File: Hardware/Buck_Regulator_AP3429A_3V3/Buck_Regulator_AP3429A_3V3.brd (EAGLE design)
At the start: 25.4 x 25.4 mm, 51 parts, among them J1 Screw Terminal, J2 POWER_JACKPOWER_JACK_SLOT_COM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, J3 Breakout Headers, U1 AP3429/A

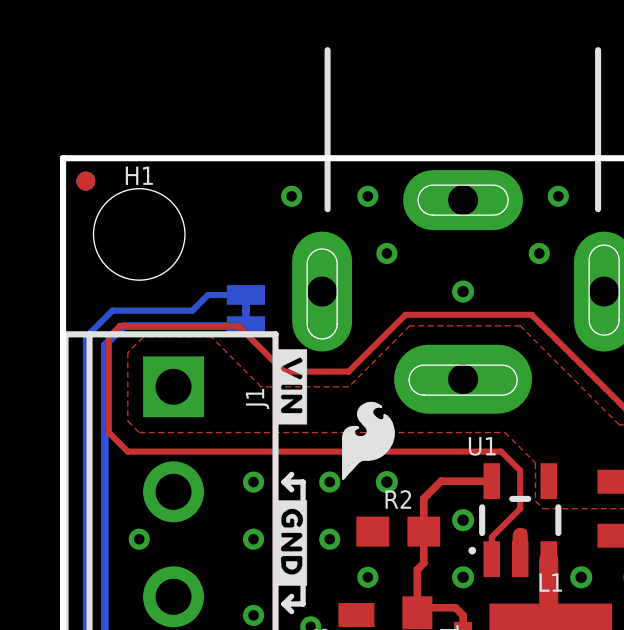
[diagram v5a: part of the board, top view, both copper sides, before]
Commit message: Changed version number in schematic, adjusted components
Moved around some silkscreen in order for easier reading on the backside; changed the version number in the schematic to v10
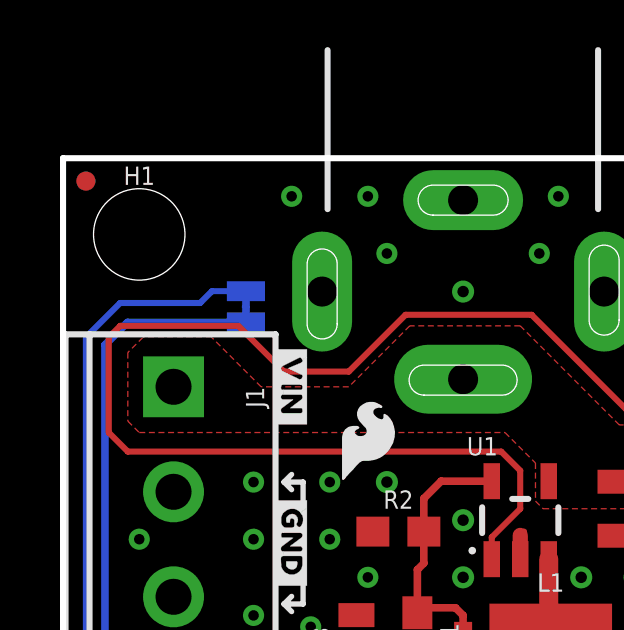
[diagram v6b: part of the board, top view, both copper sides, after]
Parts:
- moved PWR 0.13 mm to (6.10, 20.4)
- moved U$14 0.13 mm to (6.10, 23.2)
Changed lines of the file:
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@@
 <drawing>
 <settings>
-<setting alwaysvectorfont="yes"/>
+<setting alwaysvectorfont="no"/>
 <setting verticaltext="up"/>
 </settings>
@@
 <layer number="37" name="tTest" color="7" fill="1" visible="no" active="yes"/>
 <layer number="38" name="bTest" color="7" fill="1" visible="no" active="yes"/>
-<layer number="39" name="tKeepout" color="4" fill="11" visible="no" active="yes"/>
-<layer number="40" name="bKeepout" color="1" fill="11" visible="no" active="yes"/>
-<layer number="41" name="tRestrict" color="4" fill="10" visible="no" active="yes"/>
-<layer number="42" name="bRestrict" color="1" fill="10" visible="no" active="yes"/>
-<layer number="43" name="vRestrict" color="2" fill="10" visible="no" active="yes"/>
+<layer number="39" name="tKeepout" color="4" fill="11" visible="yes" active="yes"/>
+<layer number="40" name="bKeepout" color="1" fill="11" visible="yes" active="yes"/>
+<layer number="41" name="tRestrict" color="4" fill="10" visible="yes" active="yes"/>
+<layer number="42" name="bRestrict" color="1" fill="10" visible="yes" active="yes"/>
+<layer number="43" name="vRestrict" color="2" fill="10" visible="yes" active="yes"/>
 <layer number="44" name="Drills" color="7" fill="1" visible="no" active="yes"/>
 <layer number="45" name="Holes" color="7" fill="1" visible="yes" active="yes"/>
@@
 <element name="FRAME1" library="SparkFun-Aesthetics" package="CREATIVE_COMMONS" value="FRAME-LEDGER" x="-13.97" y="-41.91" smashed="yes">
 <attribute name="DESIGNER" value="M. Chodikov" x="66.04" y="-54.61" size="1.778" layer="27" display="off"/>
-<attribute name="REV" value="v01" x="66.04" y="-54.61" size="1.778" layer="27" display="off"/>
+<attribute name="REV" value="v10" x="66.04" y="-54.61" size="1.778" layer="27" display="off"/>
 </element>
 <element name="L1" library="SparkFun-Coils" package="INDUCTOR_4X4MM" value="2.2μH" x="16.256" y="8.509" smashed="yes">
@@
 <attribute name="PROD_ID" value="NDUC-13770" x="48.006" y="-15.621" size="1.778" layer="27" display="off"/>
 </element>
-<element name="PWR" library="SparkFun-Jumpers" package="SMT-JUMPER_2_NC_TRACE_SILK" package3d_urn="urn:adsk.eagle:package:39281/1" value="JUMPER-SMT_2_NC_TRACE_SILK" x="6.096" y="20.32" smashed="yes" rot="MR270">
-<attribute name="NAME" x="4.953" y="20.32" size="0.6096" layer="26" font="vector" ratio="20" rot="MR270" align="bottom-center"/>
+<element name="PWR" library="SparkFun-Jumpers" package="SMT-JUMPER_2_NC_TRACE_SILK" package3d_urn="urn:adsk.eagle:package:39281/1" value="JUMPER-SMT_2_NC_TRACE_SILK" x="6.096" y="20.447" smashed="yes" rot="MR270">
+<attribute name="NAME" x="4.953" y="20.447" size="0.6096" layer="26" font="vector" ratio="20" rot="MR270" align="bottom-center"/>
 </element>
 <element name="U1" library="SparkFun-IC-Power" package="SOT23-5" value="AP3429/A" x="15.24" y="13.335" smashed="yes">
@@
 <element name="U$13" library="output" package="#VOUT#3447" value="" x="5.334" y="7.112" smashed="yes" rot="MR90"/>
 <element name="U$15" library="output" package="#VIN#3445" value="" x="5.334" y="17.78" smashed="yes" rot="MR90"/>
-<element name="U$14" library="output" package="#PWR#3451" value="" x="6.096" y="23.114" smashed="yes" rot="MR90"/>
+<element name="U$14" library="output" package="#PWR#3451" value="" x="6.096" y="23.241" smashed="yes" rot="MR90"/>
 <element name="C1" library="SparkFun-Capacitors" package="0805" value="22uF" x="18.415" y="13.716" smashed="yes" rot="R270">
 <attribute name="NAME" x="19.304" y="13.716" size="0.6096" layer="25" font="vector" ratio="20" rot="R270" align="bottom-center"/>
@@
 <signal name="N$3">
 <contactref element="PWR" pad="1"/>
-<wire x1="6.096" y1="20.8407" x2="4.8387" y2="20.8407" width="0.2032" layer="16"/>
-<wire x1="1.651" y1="20.32" x2="0.762" y2="19.431" width="0.2032" layer="16"/>
-<wire x1="4.8387" y1="20.8407" x2="4.318" y2="20.32" width="0.2032" layer="16"/>
-<wire x1="4.318" y1="20.32" x2="1.651" y2="20.32" width="0.2032" layer="16"/>
+<wire x1="6.096" y1="20.9677" x2="4.9657" y2="20.9677" width="0.2032" layer="16"/>
+<wire x1="1.905" y1="20.574" x2="0.762" y2="19.431" width="0.2032" layer="16"/>
+<wire x1="4.9657" y1="20.9677" x2="4.572" y2="20.574" width="0.2032" layer="16"/>
+<wire x1="4.572" y1="20.574" x2="1.905" y2="20.574" width="0.2032" layer="16"/>
 <wire x1="12.485" y1="3.302" x2="13.12" y2="2.667" width="0.2032" layer="1"/>
 <wire x1="12.485" y1="3.302" x2="7.493" y2="3.302" width="0.2032" layer="1"/>
@@
 <contactref element="PWR" pad="2"/>
 <wire x1="1.397" y1="19.177" x2="1.397" y2="9.566" width="0.254" layer="16"/>
-<wire x1="6.096" y1="19.7993" x2="2.0193" y2="19.7993" width="0.254" layer="16"/>
-<wire x1="2.0193" y1="19.7993" x2="1.397" y2="19.177" width="0.254" layer="16"/>
+<wire x1="6.096" y1="19.9263" x2="2.1463" y2="19.9263" width="0.254" layer="16"/>
+<wire x1="2.1463" y1="19.9263" x2="1.397" y2="19.177" width="0.254" layer="16"/>
 <contactref element="L1" pad="P$2"/>
 <contactref element="C2" pad="1"/>

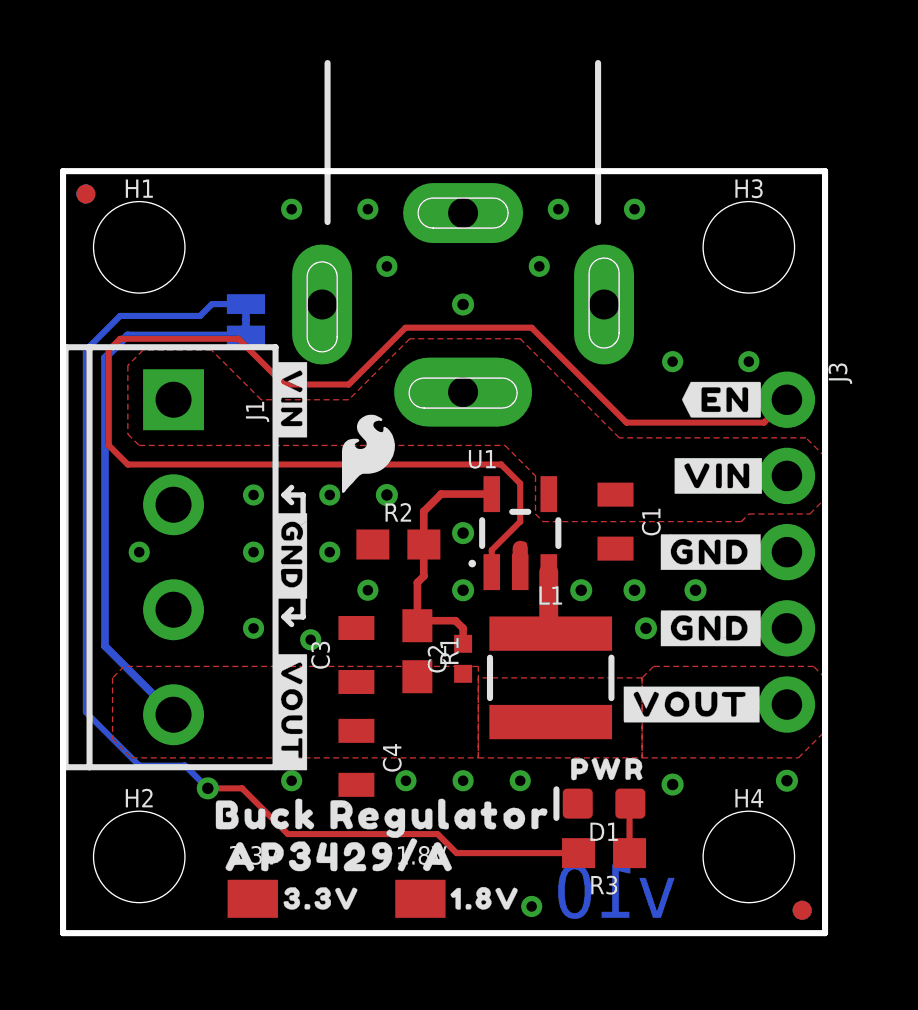
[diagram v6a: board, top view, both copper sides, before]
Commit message: Added 2 more output capacitors
Added more output capacitance to match ALC block - there was some ripple detected during testing so adding these should eliminate that. Adjusted the components on the board accordingly then matched the exact locations of said movement for each board.
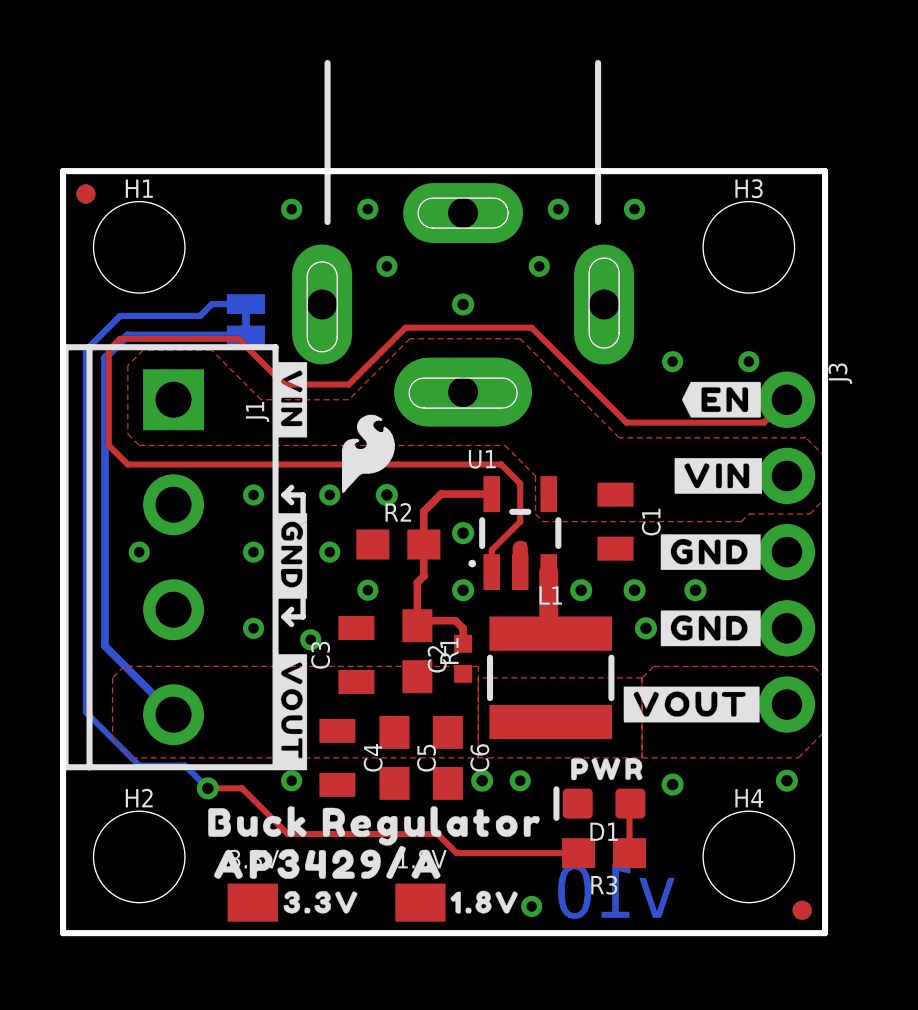
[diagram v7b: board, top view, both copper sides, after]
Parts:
- added C5: 0.1uF, SparkFun-Capacitors:0603
- added C6: 1.0uF, SparkFun-Capacitors:0603
- moved C4 0.63 mm to (9.14, 5.84)
- moved U$3 0.46 mm to (8.89, 2.29)
- moved U$2 0.36 mm to (10.4, 3.68)
- moved 1.8V 0.13 mm to (11.9, 1.02)
- moved 3.3V 0.13 mm to (6.35, 1.02)
- moved U$19 0.13 mm to (14.1, 1.02)
- moved U$23 0.13 mm to (8.64, 1.02)
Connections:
- net GND: now also C5.2, C6.2
- net VOUT: now also C5.1, C6.1
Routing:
- net GND: vias 31 -> 30
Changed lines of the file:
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@@
 <drawing>
 <settings>
-<setting alwaysvectorfont="no"/>
+<setting alwaysvectorfont="yes"/>
 <setting verticaltext="up"/>
 </settings>
@@
 <layer number="37" name="tTest" color="7" fill="1" visible="no" active="yes"/>
 <layer number="38" name="bTest" color="7" fill="1" visible="no" active="yes"/>
-<layer number="39" name="tKeepout" color="4" fill="11" visible="yes" active="yes"/>
-<layer number="40" name="bKeepout" color="1" fill="11" visible="yes" active="yes"/>
-<layer number="41" name="tRestrict" color="4" fill="10" visible="yes" active="yes"/>
-<layer number="42" name="bRestrict" color="1" fill="10" visible="yes" active="yes"/>
-<layer number="43" name="vRestrict" color="2" fill="10" visible="yes" active="yes"/>
+<layer number="39" name="tKeepout" color="4" fill="11" visible="no" active="yes"/>
+<layer number="40" name="bKeepout" color="1" fill="11" visible="no" active="yes"/>
+<layer number="41" name="tRestrict" color="4" fill="10" visible="no" active="yes"/>
+<layer number="42" name="bRestrict" color="1" fill="10" visible="no" active="yes"/>
+<layer number="43" name="vRestrict" color="2" fill="10" visible="no" active="yes"/>
 <layer number="44" name="Drills" color="7" fill="1" visible="no" active="yes"/>
 <layer number="45" name="Holes" color="7" fill="1" visible="yes" active="yes"/>
@@
 <attribute name="VALUE" x="22.098" y="19.05" size="0.6096" layer="27" font="vector" ratio="20" rot="R270"/>
 </element>
-<element name="U$2" library="output" package="BUCK_REGULATOR24" value="" x="10.668" y="3.937" smashed="yes"/>
-<element name="U$3" library="output" package="AP3429#A25" value="" x="9.271" y="2.54" smashed="yes"/>
+<element name="U$2" library="output" package="BUCK_REGULATOR24" value="" x="10.414" y="3.683" smashed="yes"/>
+<element name="U$3" library="output" package="AP3429#A25" value="" x="8.89" y="2.286" smashed="yes"/>
 <element name="U$4" library="output" package="#VOUT#3431" value="" x="20.955" y="7.62" smashed="yes"/>
 <element name="U$5" library="output" package="#GND#3432" value="" x="21.59" y="10.16" smashed="yes"/>
@@
 <attribute name="VALUE" x="1.397" y="17.78" size="0.6096" layer="27" font="vector" ratio="20" rot="R270"/>
 </element>
-<element name="1.8V" library="SparkFun-Aesthetics" package="PRODUCT_IDENT_NO_NO-SILK" value="PROD_ID_NO-PASTE_NO_SILK" x="11.938" y="1.143" smashed="yes">
-<attribute name="NAME" x="11.938" y="2.286" size="0.6096" layer="25" font="vector" ratio="20" align="bottom-center"/>
-<attribute name="VALUE" x="11.938" y="0" size="0.6096" layer="27" font="vector" ratio="20" align="top-center"/>
-</element>
-<element name="3.3V" library="SparkFun-Aesthetics" package="PRODUCT_IDENT_PASTE_NO-SILK" value="PROD_ID_PASTE_NO-SILK" x="6.35" y="1.143" smashed="yes">
-<attribute name="NAME" x="6.35" y="2.286" size="0.6096" layer="25" font="vector" ratio="20" align="bottom-center"/>
-<attribute name="VALUE" x="6.35" y="0" size="0.6096" layer="27" font="vector" ratio="20" align="top-center"/>
-</element>
-<element name="U$23" library="output" package="3#3V3441" value="" x="8.636" y="1.143" smashed="yes"/>
-<element name="U$19" library="output" package="1#8V3441" value="" x="14.097" y="1.143" smashed="yes"/>
+<element name="1.8V" library="SparkFun-Aesthetics" package="PRODUCT_IDENT_NO_NO-SILK" value="PROD_ID_NO-PASTE_NO_SILK" x="11.938" y="1.016" smashed="yes">
+<attribute name="NAME" x="11.938" y="2.159" size="0.6096" layer="25" font="vector" ratio="20" align="bottom-center"/>
+<attribute name="VALUE" x="11.938" y="-0.127" size="0.6096" layer="27" font="vector" ratio="20" align="top-center"/>
+</element>
+<element name="3.3V" library="SparkFun-Aesthetics" package="PRODUCT_IDENT_PASTE_NO-SILK" value="PROD_ID_PASTE_NO-SILK" x="6.35" y="1.016" smashed="yes">
+<attribute name="NAME" x="6.35" y="2.159" size="0.6096" layer="25" font="vector" ratio="20" align="bottom-center"/>
+<attribute name="VALUE" x="6.35" y="-0.127" size="0.6096" layer="27" font="vector" ratio="20" align="top-center"/>
+</element>
+<element name="U$23" library="output" package="3#3V3441" value="" x="8.636" y="1.016" smashed="yes"/>
+<element name="U$19" library="output" package="1#8V3441" value="" x="14.097" y="1.016" smashed="yes"/>
 <element name="U$20" library="output" package="PWR3441" value="" x="18.161" y="5.461" smashed="yes"/>
 <element name="U$25" library="output" package="#EN#3443" value="" x="22.098" y="17.78" smashed="yes"/>
@@
 <attribute name="VALUE" x="10.668" y="9.271" size="0.6096" layer="27" font="vector" ratio="20" rot="R90" align="top-center"/>
 </element>
-<element name="C4" library="SparkFun-Capacitors" package="0805" value="22uF" x="9.779" y="5.842" smashed="yes" rot="R270">
-<attribute name="NAME" x="10.668" y="5.842" size="0.6096" layer="25" font="vector" ratio="20" rot="R270" align="bottom-center"/>
-<attribute name="PROD_ID" value="CAP-14260" x="9.779" y="5.842" size="1.778" layer="27" font="vector" ratio="15" rot="R270" display="off"/>
-<attribute name="VALUE" x="8.89" y="5.842" size="0.6096" layer="27" font="vector" ratio="20" rot="R270" align="top-center"/>
+<element name="C4" library="SparkFun-Capacitors" package="0805" value="22uF" x="9.144" y="5.842" smashed="yes" rot="R270">
+<attribute name="NAME" x="10.033" y="5.842" size="0.6096" layer="25" font="vector" ratio="20" rot="R270" align="bottom-center"/>
+<attribute name="PROD_ID" value="CAP-14260" x="9.144" y="5.842" size="1.778" layer="27" font="vector" ratio="15" rot="R270" display="off"/>
+<attribute name="VALUE" x="8.255" y="5.842" size="0.6096" layer="27" font="vector" ratio="20" rot="R270" align="top-center"/>
 </element>
 <element name="U$16" library="output" package="BUCK_REGULATOR_AP3429#A3453" value="" x="1.524" y="12.827" smashed="yes" rot="MR90"/>
@@
 </element>
 <element name="J2" library="SparkFun-Connectors" package="POWER_JACK_PTH_SLOT_BOTH" value="POWER_JACKPOWER_JACK_SLOT_COMBO" x="13.335" y="24.003" smashed="yes" rot="MR90"/>
+<element name="C5" library="SparkFun-Capacitors" package="0603" value="0.1uF" x="11.049" y="5.842" smashed="yes" rot="R270">
+<attribute name="NAME" x="11.811" y="5.842" size="0.6096" layer="25" font="vector" ratio="20" rot="R270" align="bottom-center"/>
+<attribute name="PROD_ID" value="CAP-08604" x="11.049" y="5.842" size="1.778" layer="27" font="vector" ratio="15" rot="R270" display="off"/>
+<attribute name="VALUE" x="10.287" y="5.842" size="0.6096" layer="27" font="vector" ratio="20" rot="R270" align="top-center"/>
+</element>
+<element name="C6" library="SparkFun-Capacitors" package="0603" value="1.0uF" x="12.827" y="5.842" smashed="yes" rot="R270">
+<attribute name="NAME" x="13.589" y="5.842" size="0.6096" layer="25" font="vector" ratio="20" rot="R270" align="bottom-center"/>
+<attribute name="PROD_ID" value="CAP-13930" x="12.827" y="5.842" size="1.778" layer="27" font="vector" ratio="15" rot="R270" display="off"/>
+<attribute name="VALUE" x="12.065" y="5.842" size="0.6096" layer="27" font="vector" ratio="20" rot="R270" align="top-center"/>
+</element>
 </elements>
 <signals>
@@
 <via x="6.35" y="10.16" extent="1-16" drill="0.35"/>
 <via x="15.24" y="5.08" extent="1-16" drill="0.35"/>
-<via x="13.335" y="5.08" extent="1-16" drill="0.35"/>
-<via x="11.43" y="5.08" extent="1-16" drill="0.35"/>
 <via x="7.62" y="5.08" extent="1-16" drill="0.35"/>
 <via x="22.86" y="19.05" extent="1-16" drill="0.35"/>
@@
 <contactref element="R2" pad="1"/>
 <contactref element="J2" pad="GND"/>
+<contactref element="C5" pad="2"/>
+<contactref element="C6" pad="2"/>
+<via x="13.97" y="5.08" extent="1-16" drill="0.381"/>
 </signal>
 <signal name="N$1">
@@
 </polygon>
 <contactref element="R1" pad="2"/>
+<contactref element="C5" pad="1"/>
+<contactref element="C6" pad="1"/>
 </signal>
 </signals>
